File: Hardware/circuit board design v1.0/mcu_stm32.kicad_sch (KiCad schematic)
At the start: 27 parts, among them J1 Conn_01x06_Male, J4 Conn_01x04, Q1 2N7002-7-F, U1 STM32F446RETx, U2 W25Q64JVSS, U3 SDR08540M3-01, Y1 Crystal_GND24

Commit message: Finished routing
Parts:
- J4: footprint Connector_JST:JST_PH_B4B-PH-K_1x04_P2.00mm_Vertical -> Components:JST_PH_B4B-PH-K_1x04_P2.00mm_Vertical
- U1: footprint Package_QFP:LQFP-64_10x10mm_P0.5mm -> Components:LQFP-64_10x10mm_P0.5mm
- U2: footprint Package_SO:SOIC-8_5.23x5.23mm_P1.27mm -> Components:W25Q64JVSSIQ
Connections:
- net GND: no longer U3.2 (vss), U3.3 (vss), U3.4 (vss)
- net PWR_BVOLTS: now also U1.27 (PB1); no longer U1.25 (PC5)
- net at D2.2 (A), R5.1: now also U3.2 (vss), U3.3 (vss), U3.4 (vss)
- no-connect marks 31 -> 30
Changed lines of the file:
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@@
   (junction (at 90.17 90.17) (diameter 0) (color 0 0 0 0)
   )
-  (junction (at 248.92 153.67) (diameter 0) (color 0 0 0 0)
-  )
   (junction (at 116.84 21.59) (diameter 0) (color 0 0 0 0)
   )
@@
   )
   (junction (at 187.96 118.11) (diameter 0) (color 0 0 0 0)
+  )
+  (junction (at 236.22 123.19) (diameter 0) (color 0 0 0 0)
+  )
+  (junction (at 246.38 128.27) (diameter 0) (color 0 0 0 0)
   )
   (junction (at 152.4 143.51) (diameter 0) (color 0 0 0 0)
@@
   (no_connect (at 167.64 80.01))
   (no_connect (at 167.64 97.79))
-  (no_connect (at 167.64 100.33))
   (no_connect (at 167.64 59.69))
   (no_connect (at 167.64 64.77))
@@
     (stroke (width 0) (type default) (color 0 0 0 0))
   )
+  (wire (pts (xy 241.3 128.27) (xy 246.38 128.27))
+    (stroke (width 0) (type default) (color 0 0 0 0))
+  )
   (wire (pts (xy 162.56 20.32) (xy 162.56 21.59))
     (stroke (width 0) (type default) (color 0 0 0 0))
@@
     (stroke (width 0) (type default) (color 0 0 0 0))
   )
-  (wire (pts (xy 236.22 121.92) (xy 236.22 124.46))
+  (wire (pts (xy 236.22 121.92) (xy 236.22 123.19))
     (stroke (width 0) (type default) (color 0 0 0 0))
   )
@@
     (stroke (width 0) (type default) (color 0 0 0 0))
   )
+  (wire (pts (xy 167.64 100.33) (xy 173.99 100.33))
+    (stroke (width 0) (type default) (color 0 0 0 0))
+  )
   (wire (pts (xy 105.41 29.21) (xy 105.41 31.75))
     (stroke (width 0) (type default) (color 0 0 0 0))
@@
     (stroke (width 0) (type default) (color 0 0 0 0))
   )
-  (wire (pts (xy 121.92 107.95) (xy 132.08 107.95))
-    (stroke (width 0) (type default) (color 0 0 0 0))
-  )
   (wire (pts (xy 162.56 33.02) (xy 162.56 36.83))
     (stroke (width 0) (type default) (color 0 0 0 0))
@@
     (stroke (width 0) (type default) (color 0 0 0 0))
   )
+  (wire (pts (xy 236.22 123.19) (xy 236.22 124.46))
+    (stroke (width 0) (type default) (color 0 0 0 0))
+  )
   (wire (pts (xy 128.27 29.21) (xy 128.27 31.75))
     (stroke (width 0) (type default) (color 0 0 0 0))
@@
     (stroke (width 0) (type default) (color 0 0 0 0))
   )
+  (wire (pts (xy 241.3 123.19) (xy 241.3 128.27))
+    (stroke (width 0) (type default) (color 0 0 0 0))
+  )
   (wire (pts (xy 167.64 67.31) (xy 173.99 67.31))
     (stroke (width 0) (type default) (color 0 0 0 0))
@@
     (stroke (width 0) (type default) (color 0 0 0 0))
   )
-  (wire (pts (xy 248.92 153.67) (xy 248.92 128.27))
-    (stroke (width 0) (type default) (color 0 0 0 0))
-  )
   (wire (pts (xy 144.78 143.51) (xy 147.32 143.51))
     (stroke (width 0) (type default) (color 0 0 0 0))
@@
   )
   (wire (pts (xy 99.06 96.52) (xy 99.06 97.79))
+    (stroke (width 0) (type default) (color 0 0 0 0))
+  )
+  (wire (pts (xy 236.22 123.19) (xy 241.3 123.19))
     (stroke (width 0) (type default) (color 0 0 0 0))
   )
@@
     (effects (font (size 1.27 1.27)) (justify left))
   )
-  (hierarchical_label "PWR_BVOLTS" (shape input) (at 121.92 107.95 180)
-    (effects (font (size 1.27 1.27)) (justify right))
+  (hierarchical_label "PWR_BVOLTS" (shape input) (at 173.99 100.33 0)
+    (effects (font (size 1.27 1.27)) (justify left))
   )
   (hierarchical_label "SDA" (shape bidirectional) (at 191.77 115.57 0)
@@
       (effects (font (size 1.27 1.27)) (justify left))
     )
-    (property "Footprint" "Package_SO:SOIC-8_5.23x5.23mm_P1.27mm" (id 2) (at 233.68 77.47 0)
+    (property "Footprint" "Components:W25Q64JVSSIQ" (id 2) (at 233.68 77.47 0)
       (effects (font (size 1.27 1.27)) hide)
     )
@@
     (property "Reference" "J4" (id 0) (at 52.07 67.31 0))
     (property "Value" "Conn_01x04" (id 1) (at 52.07 69.85 0))
-    (property "Footprint" "Connector_JST:JST_PH_B4B-PH-K_1x04_P2.00mm_Vertical" (id 2) (at 52.07 78.74 0)
+    (property "Footprint" "Components:JST_PH_B4B-PH-K_1x04_P2.00mm_Vertical" (id 2) (at 52.07 78.74 0)
       (effects (font (size 1.27 1.27)) hide)
     )
@@
       (effects (font (size 1.27 1.27)) (justify left))
     )
-    (property "Footprint" "Package_QFP:LQFP-64_10x10mm_P0.5mm" (id 2) (at 134.62 135.89 0)
+    (property "Footprint" "Components:LQFP-64_10x10mm_P0.5mm" (id 2) (at 134.62 135.89 0)
       (effects (font (size 1.27 1.27)) (justify right) hide)
     )

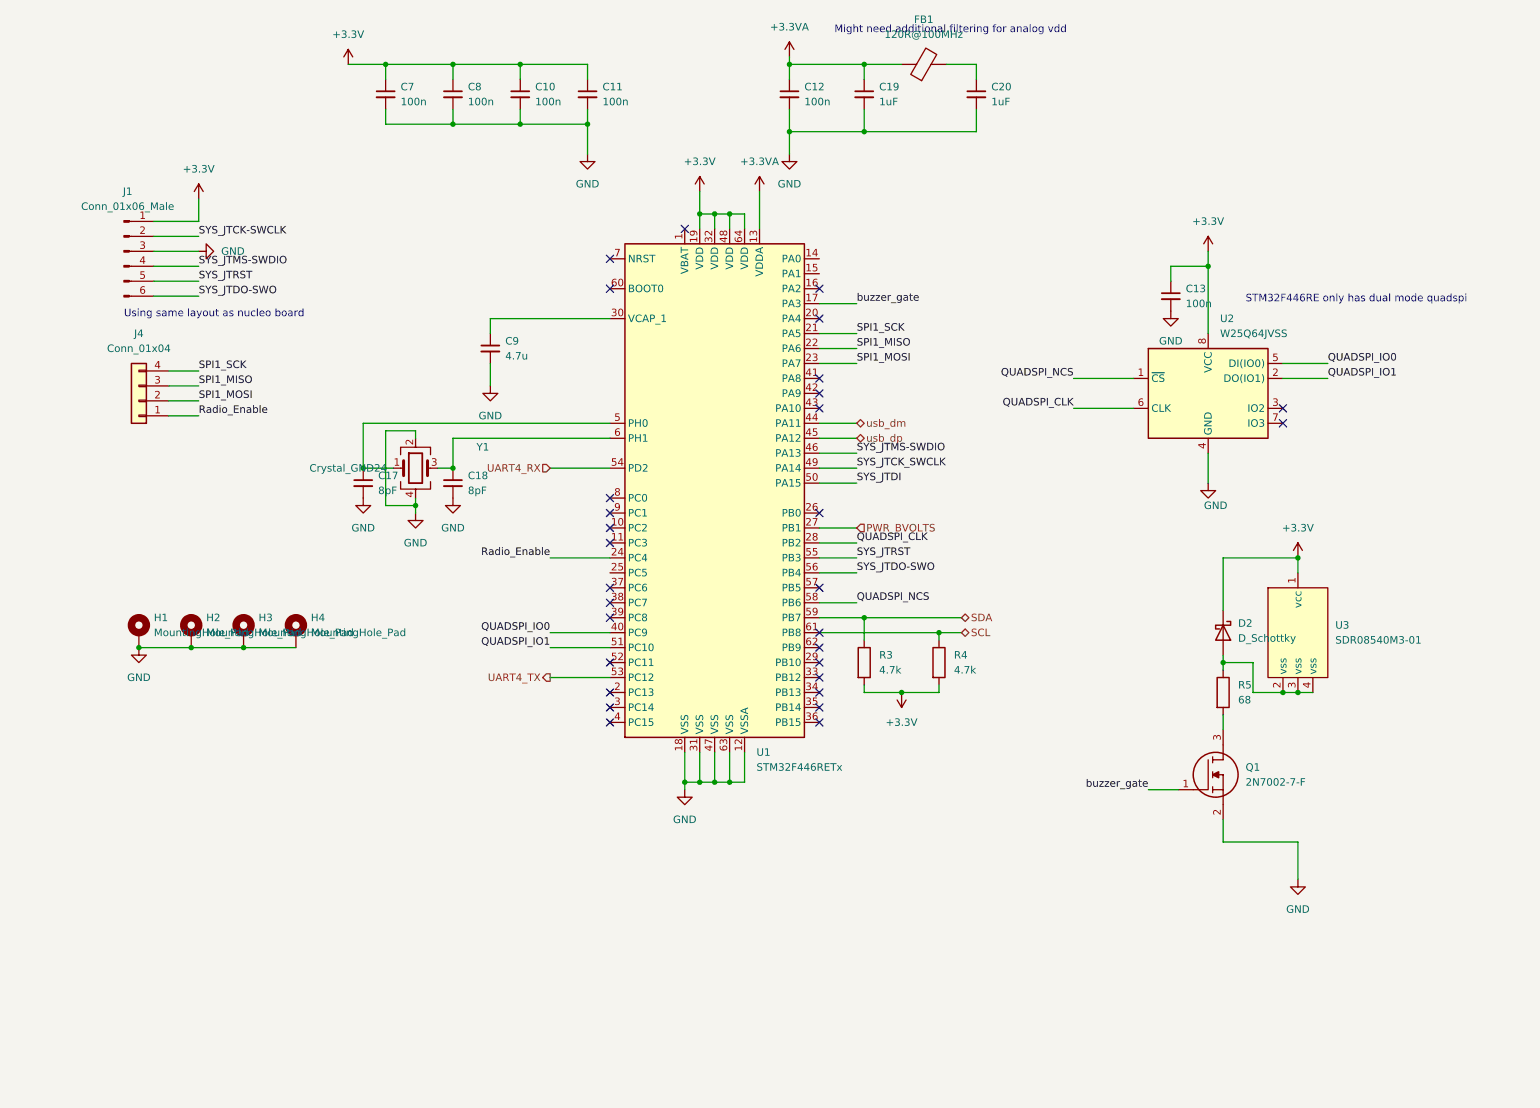
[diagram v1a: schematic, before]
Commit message: Changed connectors to horizontal
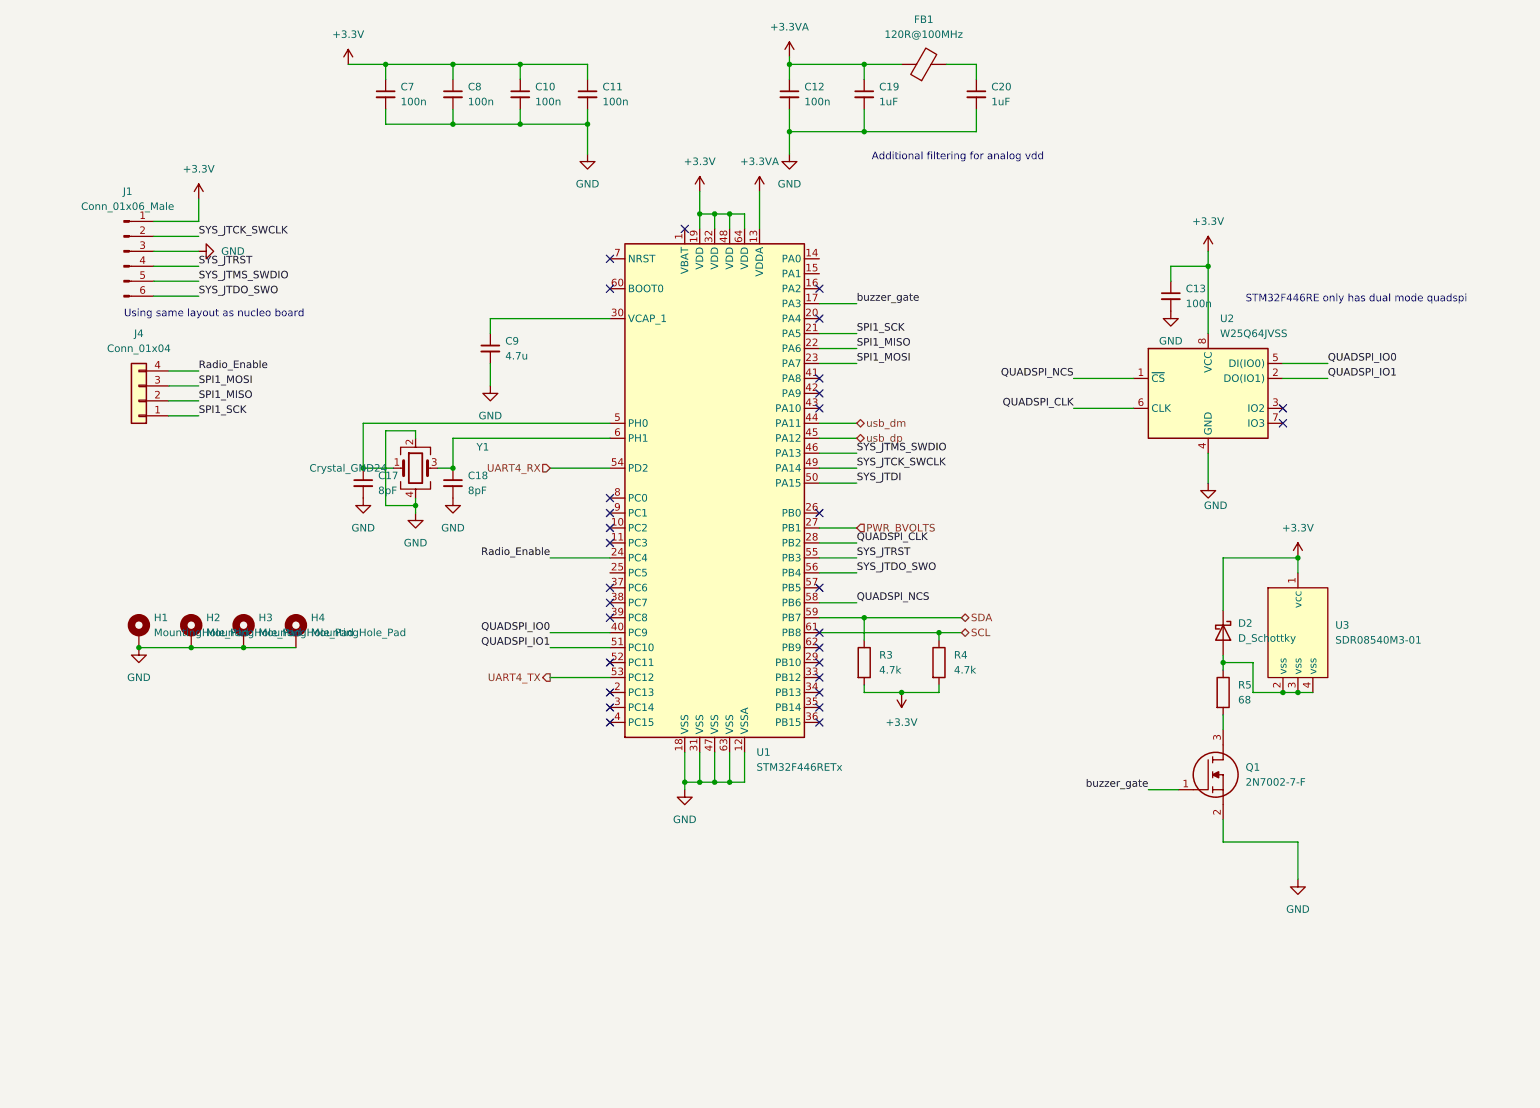
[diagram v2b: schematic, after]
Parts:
- J4: footprint Components:JST_PH_B4B-PH-K_1x04_P2.00mm_Vertical -> Components:JST_PH_S4B-PH-K_1x04_P2.00mm_Horizontal
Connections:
- net SYS_JTCK-SWCLK is gone; now on net SYS_JTCK_SWCLK: J1.2 (Pin_2)
- net Radio_Enable: now also J4.4 (Pin_4); no longer J4.1 (Pin_1)
- net SPI1_MISO: now also J4.2 (Pin_2); no longer J4.3 (Pin_3)
- net SPI1_MOSI: now also J4.3 (Pin_3); no longer J4.2 (Pin_2)
- net SPI1_SCK: now also J4.1 (Pin_1); no longer J4.4 (Pin_4)
- net SYS_JTRST: now also J1.4 (Pin_4); no longer J1.5 (Pin_5)
- net SYS_JTDO-SWO renamed SYS_JTDO_SWO
- net SYS_JTMS-SWDIO renamed SYS_JTMS_SWDIO
- net SYS_JTMS_SWDIO: now also J1.5 (Pin_5); no longer J1.4 (Pin_4)
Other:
- note added: "Additional filtering for analog vdd"
- note removed: "Might need additional filtering for analog vdd"

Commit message: Redid footprint for buzzer
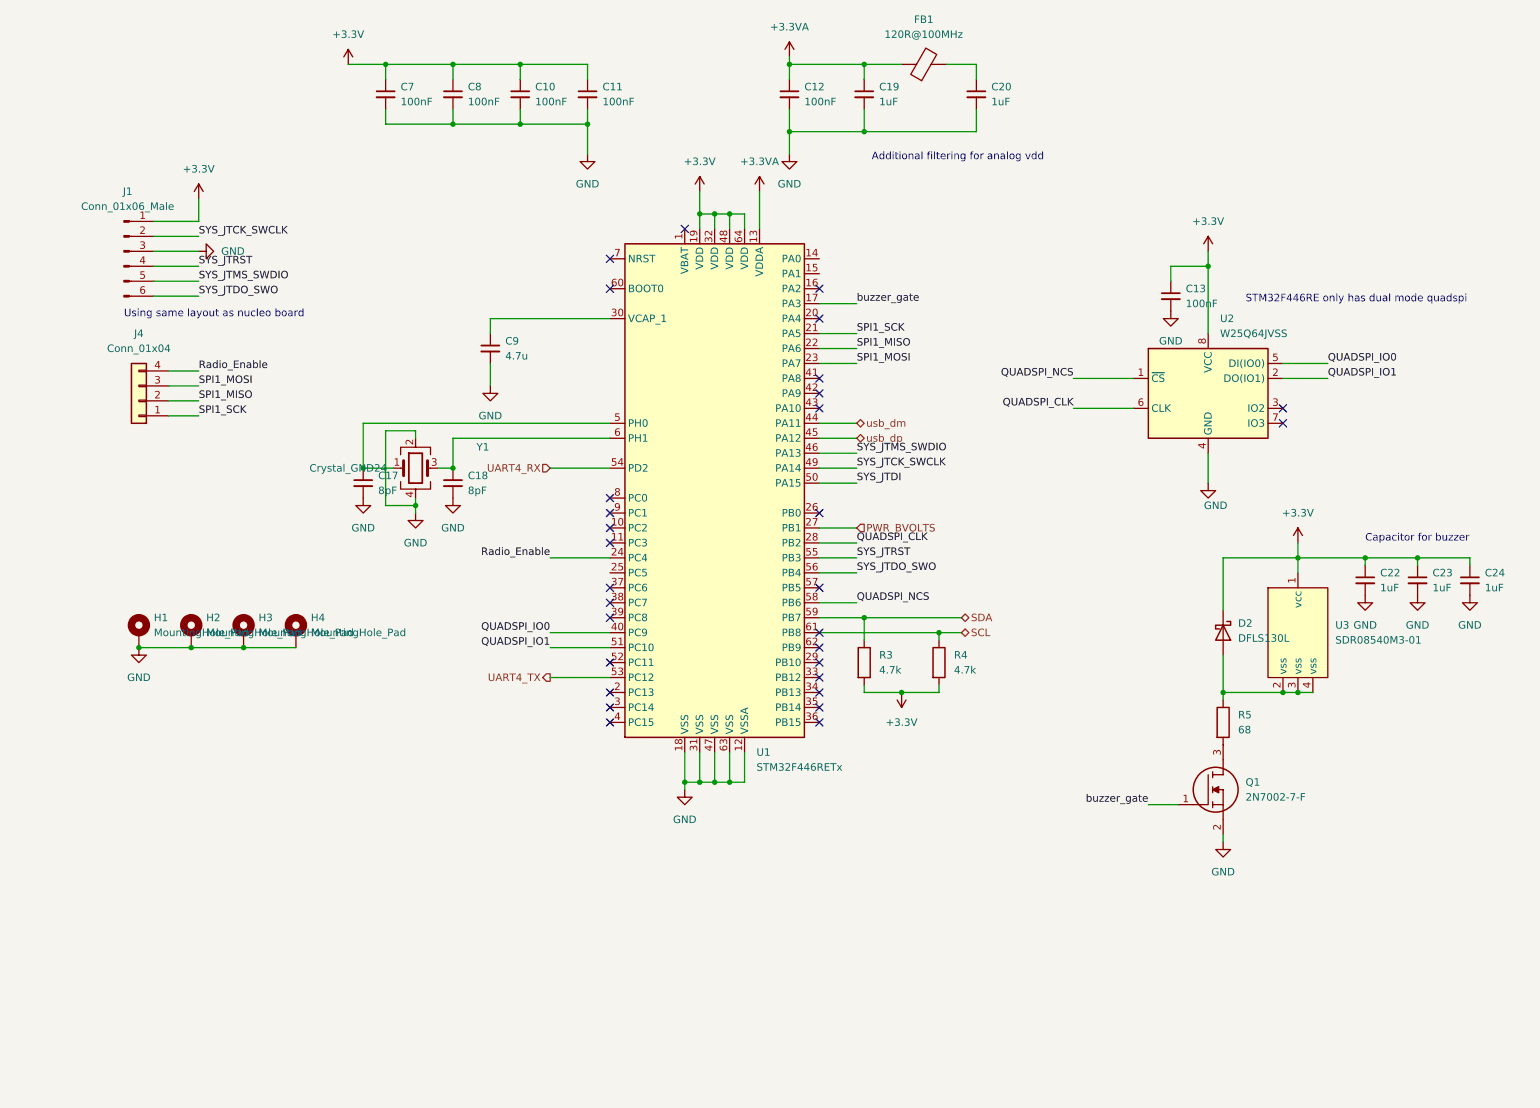
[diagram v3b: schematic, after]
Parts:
- added C22, C23, C24: 1uF, Capacitor_SMD:C_0603_1608Metric_Pad1.08x0.95mm_HandSolder, symbol Device:C_Small
- C10, C11, C12, C13, C7, C8: value 100n -> 100nF
- D2: value D_Schottky -> DFLS130L
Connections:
- net +3.3V: now also C22.1, C23.1, C24.1
- net GND: now also C22.2, C23.2, C24.2
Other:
- note added: "Capacitor for buzzer"
- moved on the sheet: Q1, R5

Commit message: Added radio connections to pcb and code
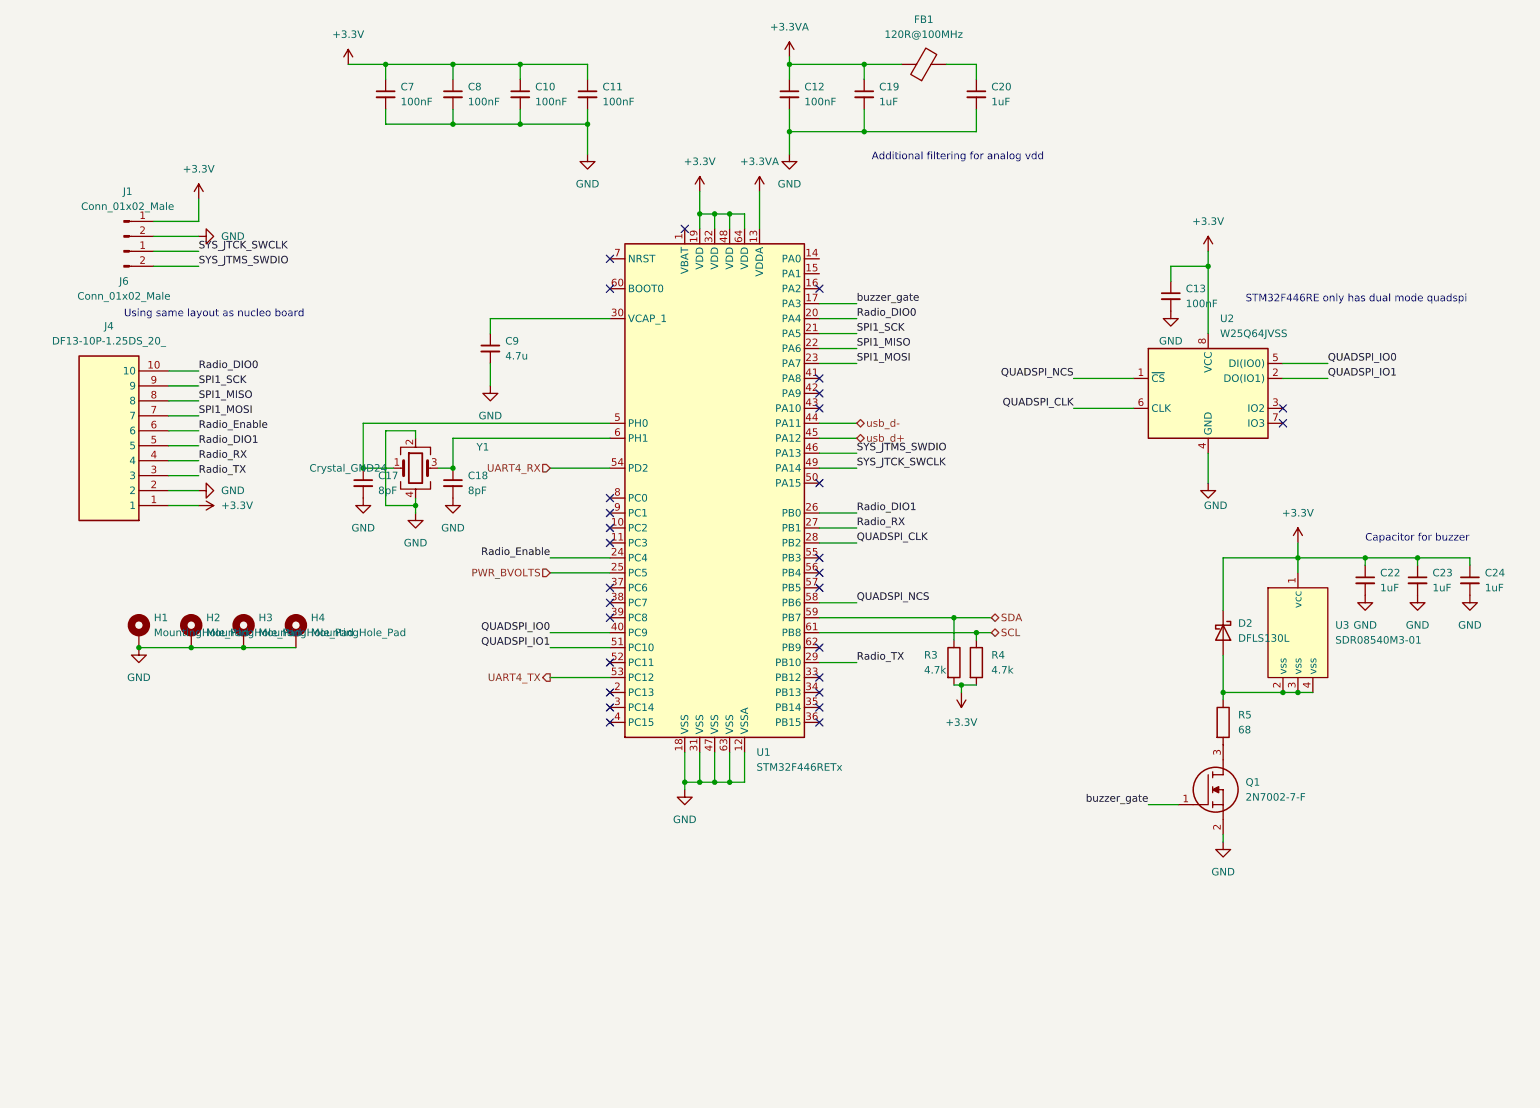
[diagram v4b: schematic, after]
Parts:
- removed J1: Conn_01x06_Male, Connector_PinHeader_2.54mm:PinHeader_2x03_P2.54mm_Vertical, symbol Connector:Conn_01x06_Male
- removed J4: Conn_01x04, Components:JST_PH_S4B-PH-K_1x04_P2.00mm_Horizontal, symbol Connector_Generic:Conn_01x04
- added J1, J6: Conn_01x02_Male, Connector_PinHeader_2.54mm:PinHeader_1x02_P2.54mm_Vertical, symbol Connector:Conn_01x02_Male
- added J4: DF13-10P-1.25DS_20_, Components:DF1310P125DS20, symbol Components:DF13-10P-1.25DS_20_
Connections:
- net +3.3V: now also J1.1 (Pin_1), J4.1
- net GND: now also J1.2 (Pin_2), J4.2
- net PWR_BVOLTS: now also U1.25 (PC5); no longer U1.27 (PB1)
- net Radio_Enable: now also J4.6
- net SPI1_MISO: now also J4.8
- net SPI1_MOSI: now also J4.7
- net SPI1_SCK: now also J4.9
- net SYS_JTCK_SWCLK: now also J6.1 (Pin_1)
- net SYS_JTMS_SWDIO: now also J6.2 (Pin_2)
- net Radio_DIO0: now reaches U1.20 (PA4)
- net Radio_DIO0: now also J4.10
- net Radio_DIO1: now reaches U1.26 (PB0)
- net Radio_DIO1: now also J4.5
- net Radio_TX: now reaches U1.29 (PB10)
- net Radio_TX: now also J4.3
- net SYS_JTDI: no longer names the net of U1.50 (PA15)
- net SYS_JTDO_SWO: no longer names the net of U1.56 (PB4)
- net SYS_JTRST: no longer names the net of U1.55 (PB3)
- net usb_dm renamed usb_d-
- net usb_dp renamed usb_d+
- new net Radio_RX: J4.4, U1.27 (PB1)
- no-connect marks 30 -> 29
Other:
- moved on the sheet: R3, R4
